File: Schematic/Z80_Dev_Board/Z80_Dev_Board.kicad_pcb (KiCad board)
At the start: 2 copper layers, 41 parts, among them J1 MCU Interface, J2 Expansion port, J3 MCU Interface 2, J4 GPIO, J5 UART B, J6 UART A, U1 74AC08, U2 62256, U3 62256, U4 74AC00, U5 74AC04, U6 Z80 CPU, U7 74HC157, U8 74AC74, U9 SC26C92, X1 4MHz, Y1 3,6864 MHz

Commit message: PCB designed
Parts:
- moved D1 162.6 mm to (127.0, 116.8)
- moved R6 157.5 mm to (134.6, 116.8)
- moved R7 129.9 mm to (105.4, 72.4), turned to 90 degrees
- moved R9 123.5 mm to (96.5, 116.8)
- moved R4 117.1 mm to (161.3, 133.3), turned to 90 degrees
- moved R10 109.9 mm to (105.4, 87.6), turned to 90 degrees
- moved C11 108.0 mm to (100.4, 121.9)
- moved R8 81.6 mm to (149.9, 118.1)
- moved J4 75.0 mm to (203.2, 111.8)
- moved C3 62.1 mm to (179.1, 55.9)
- moved C7 62.1 mm to (133.4, 55.9)
- moved C2 62.1 mm to (156.2, 55.9)
- moved J2 61.6 mm to (200.7, 61.0)
- moved U3 61.2 mm to (172.7, 61.0)
- moved U2 61.2 mm to (149.9, 61.0)
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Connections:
- J1 pad 10: /ports/a7 -> a7
- J1 pad 11: /ports/a15 -> a15
- J1 pad 12: /ports/a14 -> a14
- J1 pad 13: /ports/a13 -> a13
- J1 pad 14: /ports/a12 -> a12
- J1 pad 15: /ports/a11 -> a11
- J1 pad 16: /ports/a10 -> a10
- J1 pad 17: /ports/a9 -> a9
- J1 pad 18: /ports/a8 -> a8
- J1 pad 23: /ports/d7 -> d7
- J1 pad 24: /ports/d6 -> d6
- J1 pad 25: /ports/d5 -> d5
- J1 pad 26: /ports/d4 -> d4
- J1 pad 27: /ports/d3 -> d3
- J1 pad 28: /ports/d2 -> d2
- J1 pad 29: /ports/d1 -> d1
- J1 pad 3: /ports/a0 -> a0
- J1 pad 30: /ports/d0 -> d0
- J1 pad 4: /ports/a1 -> a1
- J1 pad 5: /ports/a2 -> a2
- J1 pad 6: /ports/a3 -> a3
- J1 pad 7: /ports/a4 -> a4
- J1 pad 8: /ports/a5 -> a5
- J1 pad 9: /ports/a6 -> a6
- J2 pad 1: /ports/d0 -> d0
- J2 pad 10: /ports/a4 -> a4
- J2 pad 11: /ports/d5 -> d5
- J2 pad 12: /ports/a5 -> a5
- J2 pad 13: /ports/d6 -> d6
- J2 pad 14: /ports/a6 -> a6
- J2 pad 15: /ports/d7 -> d7
- J2 pad 16: /ports/a7 -> a7
- J2 pad 18: /ports/a8 -> a8
- J2 pad 2: /ports/a0 -> a0
- J2 pad 20: /ports/a9 -> a9
- J2 pad 22: /ports/a10 -> a10
- J2 pad 24: /ports/a11 -> a11
- J2 pad 26: /ports/a12 -> a12
- J2 pad 28: /ports/a13 -> a13
- J2 pad 3: /ports/d1 -> d1
- J2 pad 30: /ports/a14 -> a14
- J2 pad 32: /ports/a15 -> a15
- J2 pad 4: /ports/a1 -> a1
- J2 pad 5: /ports/d2 -> d2
- J2 pad 6: /ports/a2 -> a2
- J2 pad 7: /ports/d3 -> d3
- J2 pad 8: /ports/a3 -> a3
- J2 pad 9: /ports/d4 -> d4
- U2 pad 1: /a14 -> a14
- U2 pad 10: /a0 -> a0
- U2 pad 11: /d0 -> d0
- U2 pad 12: /d1 -> d1
- U2 pad 13: /d2 -> d2
- U2 pad 15: /d3 -> d3
- U2 pad 16: /d4 -> d4
- U2 pad 17: /d5 -> d5
- U2 pad 18: /d6 -> d6
- U2 pad 19: /d7 -> d7
- U2 pad 2: /a12 -> a12
- U2 pad 21: /a10 -> a10
- U2 pad 23: /a11 -> a11
- U2 pad 24: /a9 -> a9
- U2 pad 25: /a8 -> a8
- U2 pad 26: /a13 -> a13
- U2 pad 3: /a7 -> a7
- U2 pad 4: /a6 -> a6
- U2 pad 5: /a5 -> a5
- U2 pad 6: /a4 -> a4
- U2 pad 7: /a3 -> a3
- U2 pad 8: /a2 -> a2
- U2 pad 9: /a1 -> a1
- U3 pad 1: /a14 -> a14
- U3 pad 10: /a0 -> a0
- U3 pad 11: /d0 -> d0
- U3 pad 12: /d1 -> d1
- U3 pad 13: /d2 -> d2
- U3 pad 15: /d3 -> d3
- U3 pad 16: /d4 -> d4
- U3 pad 17: /d5 -> d5
- U3 pad 18: /d6 -> d6
- U3 pad 19: /d7 -> d7
- U3 pad 2: /a12 -> a12
- U3 pad 21: /a10 -> a10
- U3 pad 23: /a11 -> a11
- U3 pad 24: /a9 -> a9
- U3 pad 25: /a8 -> a8
- U3 pad 26: /a13 -> a13
- U3 pad 3: /a7 -> a7
- U3 pad 4: /a6 -> a6
- U3 pad 5: /a5 -> a5
- U3 pad 6: /a4 -> a4
- U3 pad 7: /a3 -> a3
- U3 pad 8: /a2 -> a2
- U3 pad 9: /a1 -> a1
- U4 pad 10: /a15 -> a15
- U4 pad 4: /a15 -> a15
- U5 pad 5: /a15 -> a15
- U6 pad 1: /a11 -> a11
- U6 pad 10: /d6 -> d6
- U6 pad 12: /d2 -> d2
- U6 pad 13: /d7 -> d7
- U6 pad 14: /d0 -> d0
- U6 pad 15: /d1 -> d1
- U6 pad 2: /a12 -> a12
- U6 pad 3: /a13 -> a13
- U6 pad 30: /a0 -> a0
- U6 pad 31: /a1 -> a1
- U6 pad 32: /a2 -> a2
- U6 pad 33: /a3 -> a3
- U6 pad 34: /a4 -> a4
- U6 pad 35: /a5 -> a5
- U6 pad 36: /a6 -> a6
- U6 pad 37: /a7 -> a7
- U6 pad 38: /a8 -> a8
- U6 pad 39: /a9 -> a9
- U6 pad 4: /a14 -> a14
- U6 pad 40: /a10 -> a10
- U6 pad 5: /a15 -> a15
- U6 pad 7: /d4 -> d4
- U6 pad 8: /d3 -> d3
- U6 pad 9: /d5 -> d5
- U9 pad 18: /ports/d1 -> d1
- U9 pad 19: /ports/d3 -> d3
- U9 pad 2: /ports/a0 -> a0
- U9 pad 20: /ports/d5 -> d5
- U9 pad 21: /ports/d7 -> d7
- U9 pad 25: /ports/d6 -> d6
- U9 pad 26: /ports/d4 -> d4
- U9 pad 27: /ports/d2 -> d2
- U9 pad 28: /ports/d0 -> d0
- U9 pad 4: /ports/a1 -> a1
- U9 pad 6: /ports/a2 -> a2
- U9 pad 7: /ports/a3 -> a3
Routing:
- net +5V: track 0.00 -> 457.7 mm, vias 0 -> 9
- net d3: track 0.00 -> 200.0 mm, vias 0 -> 8
- net d4: track 0.00 -> 195.9 mm, vias 0 -> 7
- net a15: track 0.00 -> 195.8 mm, vias 0 -> 4
- net a0: track 0.00 -> 188.7 mm, vias 0 -> 2
- net d5: track 0.00 -> 186.0 mm, vias 0 -> 6
- net d0: track 0.00 -> 183.5 mm, vias 0 -> 4
- net d1: track 0.00 -> 181.1 mm, vias 0 -> 5
- net a1: track 0.00 -> 180.5 mm, vias 0 -> 4
- net a2: track 0.00 -> 177.9 mm, vias 0 -> 4
- net ~RESET: track 0.00 -> 174.1 mm, vias 0 -> 5
- net d2: track 0.00 -> 171.8 mm, vias 0 -> 4
- net a3: track 0.00 -> 171.6 mm, vias 0 -> 5
- net d6: track 0.00 -> 167.0 mm, vias 0 -> 7
- net d7: track 0.00 -> 166.2 mm, vias 0 -> 7
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- added copper zone on F.Cu, net GND

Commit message: PCB RC1
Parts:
- added REF**: OSHW-Logo_5.7x6mm_SilkScreen, Symbol:OSHW-Logo_5.7x6mm_SilkScreen, F.Cu at (182.4, 99.6)
- added REF**: KiCad-Logo2_5mm_SilkScreen, Symbol:KiCad-Logo2_5mm_SilkScreen, F.Cu at (170.7, 99.6)
- added TP1: TestPoint, TestPoint:TestPoint_Keystone_5005-5009_Compact, F.Cu at (189.2, 101.6)
- moved C4 1.82 mm to (104.2, 57.1)
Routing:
- net IORQ: track 0.00 -> 26.3 mm
- net GND: track 75.2 -> 85.4 mm, vias 1 -> 2
- net ~EXT_IRQ: track 87.8 -> 89.2 mm
- added copper zone on B.Cu, net GND
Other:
- board outline added: 116.8 x 97.8 mm
- board text added: "GND"
- board text added: "M1"
- board text added: "UART A"
- board text added: "UART B"
- board text added: "VCC"
- board text added: "Z80 Dev Board v.01 Author: Dawid Buchwald"
- board text added: "Z80_CLK"
- board text added: "a0"
- board text added: "a1"
- board text added: "a10"
- board text added: "a11"
- board text added: "a12"
- board text added: "a13"
- board text added: "a14"
- board text added: "a15"
- board text added: "a2"
- board text added: "a3"
- board text added: "a4"
- board text added: "a5"
- board text added: "a6"
- board text added: "a7"
- board text added: "a8"
- board text added: "a9"
- board text added: "d0"
- board text added: "d1"
- board text added: "d2"
- board text added: "d3"
- board text added: "d4"
- board text added: "d5"
- board text added: "d6"
- board text added: "d7"
- board text added: "ip2"
- board text added: "ip3"
- board text added: "ip4"
- board text added: "ip5"
- board text added: "ip6"
- board text added: "op2"
- board text added: "op3"
- board text added: "op4"
- board text added: "op5"
- board text added: "op6"
- board text added: "op7"
- board text added: "~ACK"
- board text added: "~BUSACK"
- board text added: "~BUSRQ"
- board text added: "~HALT"
- board text added: "~IORQ"
- board text added: "~IRQ"
- board text added: "~MREQ"
- board text added: "~NMI"
- board text added: "~RD"
- board text added: "~RESET"
- board text added: "~RFSH"
- board text added: "~WR"

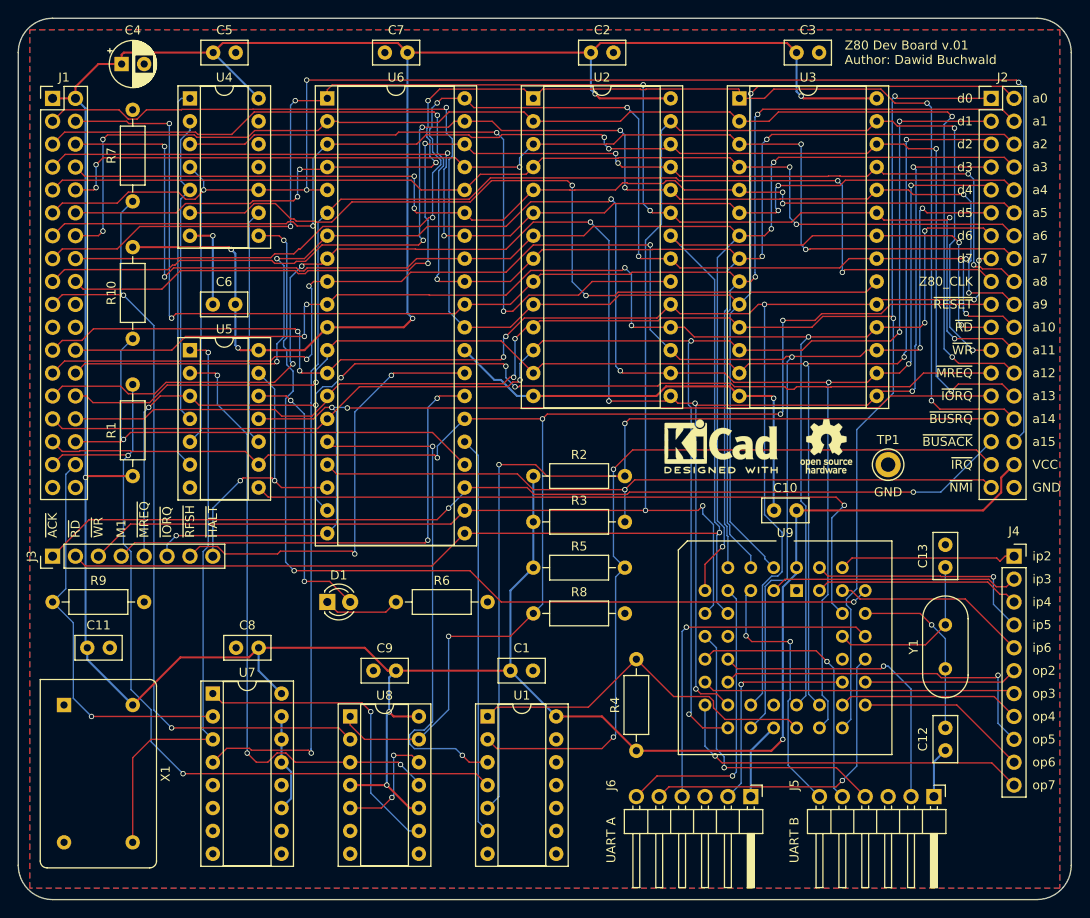
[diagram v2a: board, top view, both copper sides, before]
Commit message: Small cosmetic updates to PCB
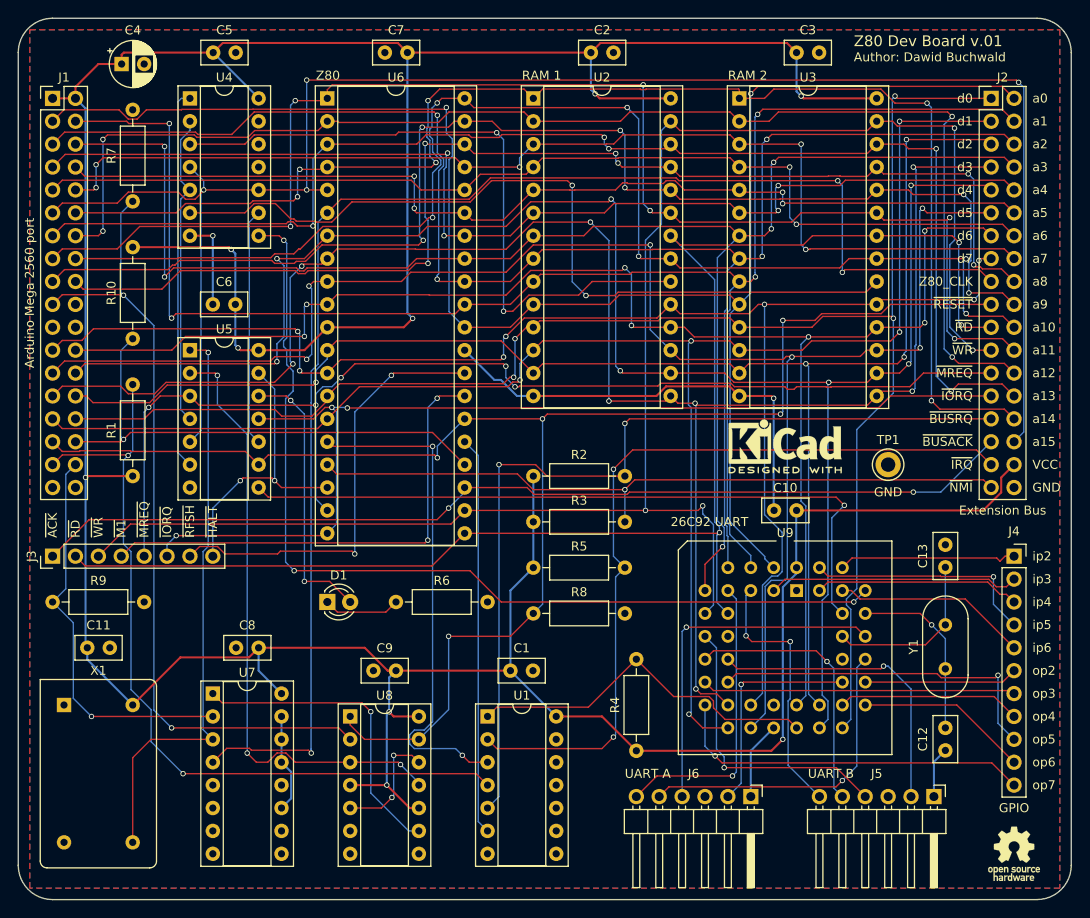
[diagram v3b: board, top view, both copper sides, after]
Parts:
- moved REF** 49.8 mm to (203.2, 144.8)
- moved REF** 7.11 mm to (177.8, 99.6)
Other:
- board text added: "26C92 UART"
- board text added: "Arduino Mega 2560 port"
- board text added: "Author: Dawid Buchwald"
- board text added: "Extension Bus"
- board text added: "GPIO"
- board text added: "RAM 1"
- board text added: "RAM 2"
- board text added: "Z80"
- board text added: "Z80 Dev Board v.01"
- board text added: "~M1"
- board text removed: "M1"
- board text removed: "Z80 Dev Board v.01 Author: Dawid Buchwald"
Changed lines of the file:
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@@
   (general
     (thickness 1.6)
-    (drawings 67)
+    (drawings 75)
     (tracks 1591)
     (zones 0)
@@
   )
   (module Symbol:OSHW-Logo_5.7x6mm_SilkScreen (layer F.Cu)
-    (at 182.372 99.568)
+    (at 203.2 144.78)
     (descr "Open Source Hardware Logo")
     (tags "Logo OSHW")
@@
   )
   (module Symbol:KiCad-Logo2_5mm_SilkScreen (layer F.Cu)
-    (at 170.688 99.568)
+    (at 177.8 99.568)
     (descr "KiCad Logo")
     (tags "Logo KiCad")
@@
     (descr "Through hole angled pin header, 1x06, 2.54mm pitch, 6mm pin length, single row")
     (tags "Through hole angled pin header THT 1x06 2.54mm single row")
-    (fp_text reference J5 (at -1.27 15.494 90) (layer F.SilkS)
+    (fp_text reference J5 (at -2.54 6.35 180) (layer F.SilkS)
       (effects (font (size 1 1) (thickness 0.15)))
     )
@@
     (descr "Through hole angled pin header, 1x06, 2.54mm pitch, 6mm pin length, single row")
     (tags "Through hole angled pin header THT 1x06 2.54mm single row")
-    (fp_text reference J6 (at -1.27 15.494 90) (layer F.SilkS)
+    (fp_text reference J6 (at -2.54 6.35 180) (layer F.SilkS)
       (effects (font (size 1 1) (thickness 0.15)))
     )
@@
     (descr "Oscillator, DIP14, http://cdn-reichelt.de/documents/datenblatt/B400/OSZI.pdf")
     (tags oscillator)
-    (fp_text reference X1 (at 7.62 -11.26 90) (layer F.SilkS)
+    (fp_text reference X1 (at -3.81 -3.81 180) (layer F.SilkS)
       (effects (font (size 1 1) (thickness 0.15)))
     )
@@
     )
   )
+  (gr_text "Author: Dawid Buchwald" (at 185.42 56.388) (layer F.SilkS)
+    (effects (font (size 1 1) (thickness 0.15)) (justify left))
+  )
+  (gr_text "Extension Bus" (at 201.93 106.68) (layer F.SilkS)
+    (effects (font (size 1 1) (thickness 0.15)))
+  )
+  (gr_text "Arduino Mega 2560 port" (at 93.98 82.55 90) (layer F.SilkS)
+    (effects (font (size 1 1) (thickness 0.15)))
+  )
+  (gr_text "26C92 UART" (at 165.1 107.95) (layer F.SilkS)
+    (effects (font (size 1 1) (thickness 0.15)) (justify left))
+  )
+  (gr_text "RAM 2" (at 171.45 58.42) (layer F.SilkS)
+    (effects (font (size 1 1) (thickness 0.15)) (justify left))
+  )
+  (gr_text "RAM 1" (at 148.59 58.42) (layer F.SilkS)
+    (effects (font (size 1 1) (thickness 0.15)) (justify left))
+  )
+  (gr_text Z80 (at 125.73 58.42) (layer F.SilkS)
+    (effects (font (size 1 1) (thickness 0.15)) (justify left))
+  )
+  (gr_text GPIO (at 203.2 139.7) (layer F.SilkS)
+    (effects (font (size 1 1) (thickness 0.15)))
+  )
   (gr_text GND (at 189.23 104.648) (layer F.SilkS)
     (effects (font (size 1 1) (thickness 0.15)))
   )
-  (gr_text "UART B" (at 178.816 143.256 90) (layer F.SilkS)
+  (gr_text "UART B" (at 182.88 135.89) (layer F.SilkS)
     (effects (font (size 1 1) (thickness 0.15)))
   )
-  (gr_text "UART A" (at 158.496 143.256 90) (layer F.SilkS)
+  (gr_text "UART A" (at 162.56 135.89) (layer F.SilkS)
     (effects (font (size 1 1) (thickness 0.15)))
   )
@@
     (effects (font (size 1 1) (thickness 0.15)) (justify left))
   )
-  (gr_text "Z80 Dev Board v.01\nAuthor: Dawid Buchwald" (at 184.404 55.88) (layer F.SilkS)
-    (effects (font (size 1 1) (thickness 0.15)) (justify left))
+  (gr_text "Z80 Dev Board v.01" (at 185.42 54.61) (layer F.SilkS)
+    (effects (font (size 1.2 1.2) (thickness 0.15)) (justify left))
   )
   (gr_text ~HALT (at 114.3 109.728 90) (layer F.SilkS)
@@
     (effects (font (size 1 1) (thickness 0.15)) (justify left))
   )
-  (gr_text M1 (at 104.14 109.728 90) (layer F.SilkS)
+  (gr_text ~M1 (at 104.14 109.728 90) (layer F.SilkS)
     (effects (font (size 1 1) (thickness 0.15)) (justify left))
   )

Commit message: Completed PCB rework
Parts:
- J1: moved to B.Cu
- J2: footprint Connector_PinHeader_2.54mm:PinHeader_2x18_P2.54mm_Vertical -> Connector_PinSocket_2.54mm:PinSocket_2x18_P2.54mm_Vertical
- J3: footprint Connector_PinHeader_2.54mm:PinHeader_1x08_P2.54mm_Vertical -> Connector_PinSocket_2.54mm:PinSocket_1x08_P2.54mm_Vertical
- moved REF** 3.82 mm to (174.0, 99.8)
- moved J1 2.54 mm to (94.0, 61.0), turned to 180 degrees
- moved J2 2.54 mm to (203.2, 61.0)
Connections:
- J1 pad 10: a7 -> a6
- J1 pad 11: a15 -> a14
- J1 pad 12: a14 -> a15
- J1 pad 13: a13 -> a12
- J1 pad 14: a12 -> a13
- J1 pad 15: a11 -> a10
- J1 pad 16: a10 -> a11
- J1 pad 17: a9 -> a8
- J1 pad 18: a8 -> a9
- J1 pad 19: CLKSEL -> Net-(J1-Pad19)
- J1 pad 20: Net-(J1-Pad20) -> CLKSEL
- J1 pad 23: d7 -> d6
- J1 pad 24: d6 -> d7
- J1 pad 25: d5 -> d4
- J1 pad 26: d4 -> d5
- J1 pad 27: d3 -> d2
- J1 pad 28: d2 -> d3
- J1 pad 29: d1 -> d0
- J1 pad 3: a0 -> a1
- J1 pad 30: d0 -> d1
- J1 pad 31: ~RESET -> ~WAIT
- J1 pad 32: ~WAIT -> ~RESET
- J1 pad 33: ~DBG_BUSRQ -> DBG_CLK
- J1 pad 34: DBG_CLK -> ~DBG_BUSRQ
- J1 pad 4: a1 -> a0
- J1 pad 5: a2 -> a3
- J1 pad 6: a3 -> a2
- J1 pad 7: a4 -> a5
- J1 pad 8: a5 -> a4
- J1 pad 9: a6 -> a7
- J2 pad 1: d0 -> a0
- J2 pad 10: a4 -> d4
- J2 pad 11: d5 -> a5
- J2 pad 12: a5 -> d5
- J2 pad 13: d6 -> a6
- J2 pad 14: a6 -> d6
- J2 pad 15: d7 -> a7
- J2 pad 16: a7 -> d7
- J2 pad 17: Z80_CLK -> a8
- J2 pad 18: a8 -> Z80_CLK
- J2 pad 19: ~RESET -> a9
- J2 pad 2: a0 -> d0
- J2 pad 20: a9 -> ~RESET
- J2 pad 21: ~RD -> a10
- J2 pad 22: a10 -> ~RD
- J2 pad 23: ~WR -> a11
- J2 pad 24: a11 -> ~WR
- J2 pad 25: ~MREQ -> a12
- J2 pad 26: a12 -> ~MREQ
- J2 pad 27: ~IORQ -> a13
- J2 pad 28: a13 -> ~IORQ
- J2 pad 29: ~EXT_BUSRQ -> a14
- J2 pad 3: d1 -> a1
- J2 pad 30: a14 -> ~EXT_BUSRQ
- J2 pad 31: ~BUSACK -> a15
- J2 pad 32: a15 -> ~BUSACK
- J2 pad 33: ~EXT_IRQ -> +5V
- J2 pad 34: +5V -> ~EXT_IRQ
- J2 pad 35: ~NMI -> GND
- J2 pad 36: GND -> ~NMI
- J2 pad 4: a1 -> d1
- J2 pad 5: d2 -> a2
- J2 pad 6: a2 -> d2
- J2 pad 7: d3 -> a3
- J2 pad 8: a3 -> d3
- J2 pad 9: d4 -> a4
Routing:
- net +5V: track 457.4 -> 467.5 mm
- net ~DBG_BUSRQ: track 89.5 -> 94.6 mm
- net d7: track 166.2 -> 171.3 mm
- net d4: track 195.9 -> 201.0 mm
- net d0: track 183.5 -> 188.6 mm
- net a7: track 121.9 -> 127.0 mm
- net a3: track 171.6 -> 176.6 mm
- net a2: track 177.9 -> 183.0 mm
- net a12: track 146.2 -> 151.3 mm
- net a0: track 188.7 -> 193.8 mm
- net ~WAIT: track 56.9 -> 62.0 mm
- net a6: track 115.9 -> 121.0 mm
- net a5: track 113.0 -> 118.1 mm
- net a4: track 122.8 -> 127.9 mm
- net CLKSEL: track 90.0 -> 95.1 mm
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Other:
- board size 116.8 x 97.8 mm -> 120.7 x 97.8 mm
- board text added: "A0"
- board text added: "A1"
- board text added: "A10"
- board text added: "A11"
- board text added: "A12"
- board text added: "A13"
- board text added: "A14"
- board text added: "A15"
- board text added: "A2"
- board text added: "A3"
- board text added: "A4"
- board text added: "A5"
- board text added: "A6"
- board text added: "A7"
- board text added: "A8"
- board text added: "A9"
- board text added: "D0"
- board text added: "D1"
- board text added: "D2"
- board text added: "D3"
- board text added: "D4"
- board text added: "D5"
- board text added: "D6"
- board text added: "D7"
- board text added: "J1"
- board text removed: "a0"
- board text removed: "a1"
- board text removed: "a10"
- board text removed: "a11"
- board text removed: "a12"
- board text removed: "a13"
- board text removed: "a14"
- board text removed: "a15"
- board text removed: "a2"
- board text removed: "a3"
- board text removed: "a4"
- board text removed: "a5"
- board text removed: "a6"
- board text removed: "a7"
- board text removed: "a8"
- board text removed: "a9"
- board text removed: "d0"
- board text removed: "d1"
- board text removed: "d2"
- board text removed: "d3"
- board text removed: "d4"
- board text removed: "d5"
- board text removed: "d6"
- board text removed: "d7"

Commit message: PCB RC2 with gerbers
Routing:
- net DBG_CLK: track 44.2 -> 46.8 mm

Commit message: PCB RC3 with gerbers
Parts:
- added J7: GPIO Output, Connector_PinSocket_2.54mm:PinSocket_1x06_P2.54mm_Vertical, F.Cu at (203.2, 127.0)
- J6: renamed from J4; value GPIO -> GPIO Input; footprint Connector_PinSocket_2.54mm:PinSocket_1x11_P2.54mm_Vertical -> Connector_PinSocket_2.54mm:PinSocket_1x05_P2.54mm_Vertical
- moved J6 1.27 mm to (203.2, 110.5)
- moved REF** 1.27 mm to (203.2, 146.1)
- renumbered J3 to J2, J2 to J3, J5 to J4, J6 to J5
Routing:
- net /ports/op7: track 40.7 -> 43.3 mm
- net /ports/op4: track 20.4 -> 22.9 mm
- net /ports/op6: track 19.1 -> 21.7 mm
- net /ports/op5: track 38.8 -> 41.3 mm
- net /ports/op3: track 34.8 -> 36.1 mm
- net /ports/ip5: track 26.1 -> 25.2 mm
- net /ports/ip6: track 21.7 -> 21.2 mm
- net /ports/ip4: track 22.9 -> 22.4 mm
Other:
- board size 120.7 x 97.8 mm -> 120.7 x 98.3 mm
- board text added: "GPIO Input"
- board text added: "GPIO Output"
- board text added: "IP2"
- board text added: "IP3"
- board text added: "IP4"
- board text added: "IP5"
- board text added: "IP6"
- board text added: "OP2"
- board text added: "OP3"
- board text added: "OP4"
- board text added: "OP5"
- board text added: "OP6"
- board text added: "OP7"
- board text removed: "GPIO"
- board text removed: "ip2"
- board text removed: "ip3"
- board text removed: "ip4"
- board text removed: "ip5"
- board text removed: "ip6"
- board text removed: "op2"
- board text removed: "op3"
- board text removed: "op4"
- board text removed: "op5"
- board text removed: "op6"
- board text removed: "op7"
